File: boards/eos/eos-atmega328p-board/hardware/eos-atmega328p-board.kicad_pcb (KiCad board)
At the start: 2 copper layers, 68.6 x 53.3 mm, 71 parts, among them J1 USB-C, J2 7-12V, J3 D0-D7, J4 D8-SCL, J5 POWER, J6 A0-A5, J7 ICSP, SW1 RESET, U1 USBLC6-2SC6, U10 SN74LVC1G07, U2 AP63205, U3 TPS2116, U4 AP2112K-3.3, U5 CH340C, U6 ATmega328P-AU, U7 SN74LVC1G17, U8 SN74LVC1G17, U9 SN74LVC1G17, Y1 16MHz

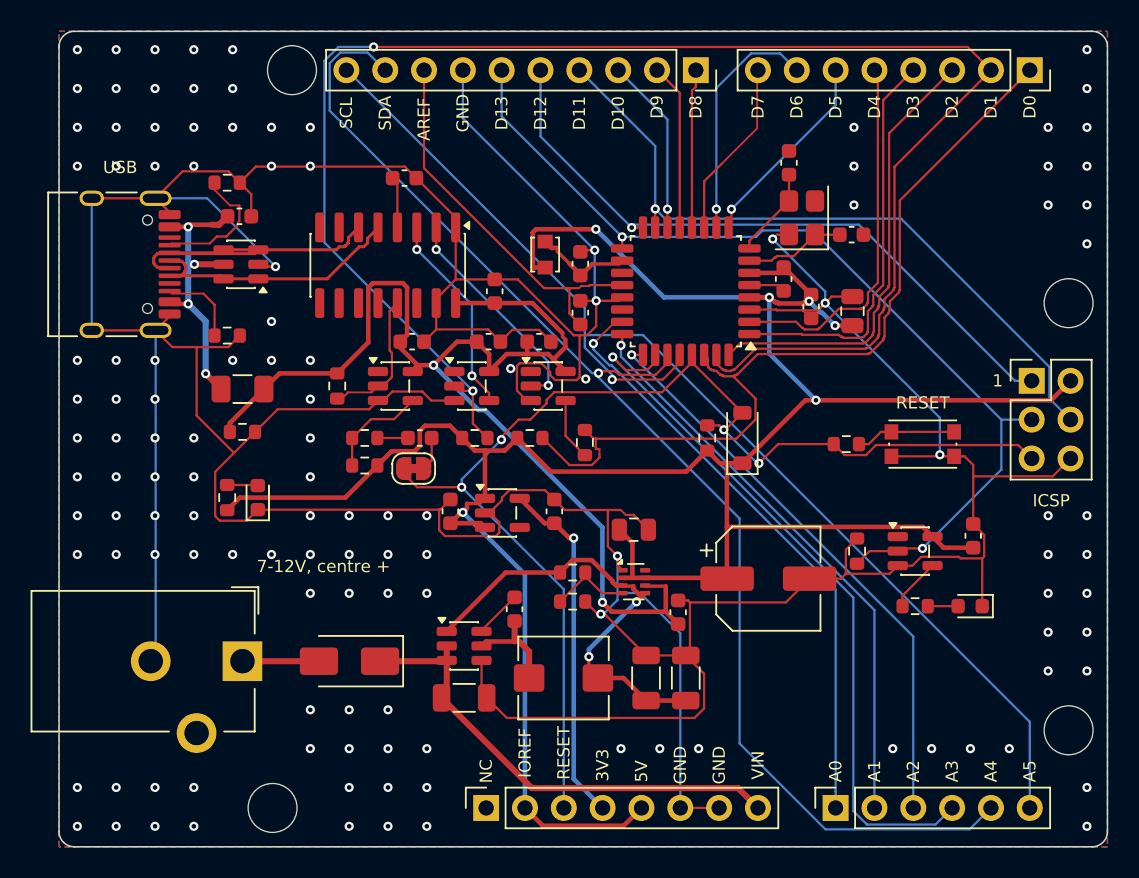
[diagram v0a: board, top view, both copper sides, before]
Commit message: fix(boards): rebuild the ten boards made before the no-via-in-pad rule (#55)
PR #64's generator keeps vias out of surface pads (a chip's exposed pad
aside) and 0.1 mm from their own net's pads. Ten boards on master were built
before that rule and had 34 pads with a via in or beside them. They are
rebuilt with the same generator: ATmega328P, RA2E1, KE16Z, KL25, STM32 64,
ESP32 DevKit, Learn RP2350, LPC55S69, CM4 Base and CM5 Base. Each builds at
ERC 0, DRC errors 0, unconnected 0 and parity 0, with the same parts, values,
nets and positions and the same DRC warnings as before.

Where the router could no longer close a short link without a via in a pad,
or left a ground pad without a good path to a via, the design files use
routing options only: priority routes, fanout_first, ground_vias, and a
bottom-layer router keep-out under KL25's crystal (so RESET_b no longer runs
under it). ViaInPadTest drops BUILT_BEFORE_THE_RULE; it now allows only Learn
RP2350's two Raspberry Pi reference vias, named by position. READMEs, TASKS
and CHANGELOG follow the rebuilt copper. Independent verification: three
rounds; the owner adopted a two-layer pour-island criterion (TASKS.md).

Part of #55.
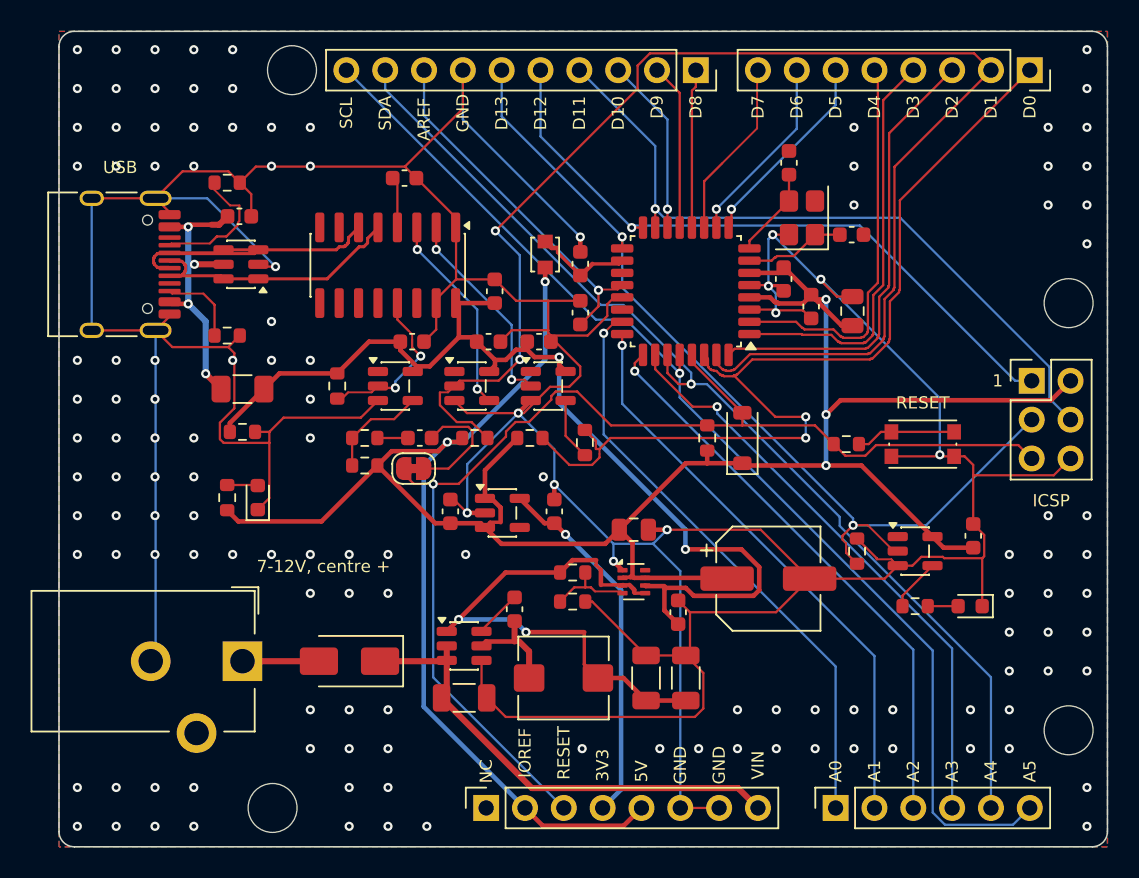
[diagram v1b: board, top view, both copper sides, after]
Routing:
- net /D1: track 107.8 -> 91.7 mm
- net /A4_SDA: track 85.1 -> 69.2 mm
- net /A3: track 47.3 -> 38.6 mm
- net /VUSB: track 76.8 -> 68.6 mm
- net /D0: track 56.7 -> 63.5 mm, vias 0 -> 2
- net /DTR_JP: track 2.22 -> 7.81 mm
- net /5V_REG: track 29.5 -> 35.0 mm
- net /A5_SCL: track 78.1 -> 73.9 mm
- net /D6: track 15.8 -> 12.5 mm
- net GND: track 348.7 -> 351.8 mm, vias 128 -> 137
- net +5V: track 178.1 -> 175.5 mm, vias 6 -> 5
- net /AREF: track 25.4 -> 23.6 mm, vias 0 -> 1
- net /CH_DTR: track 9.27 -> 11.1 mm, vias 0 -> 2
- net /D4: track 24.3 -> 25.9 mm
- net /CH_TX: track 14.5 -> 13.4 mm
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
